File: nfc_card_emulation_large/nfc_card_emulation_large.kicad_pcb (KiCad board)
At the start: 2 copper layers, 54 x 85.7 mm, 13 parts, among them J1 Qwiic, U2 NT3H2x11

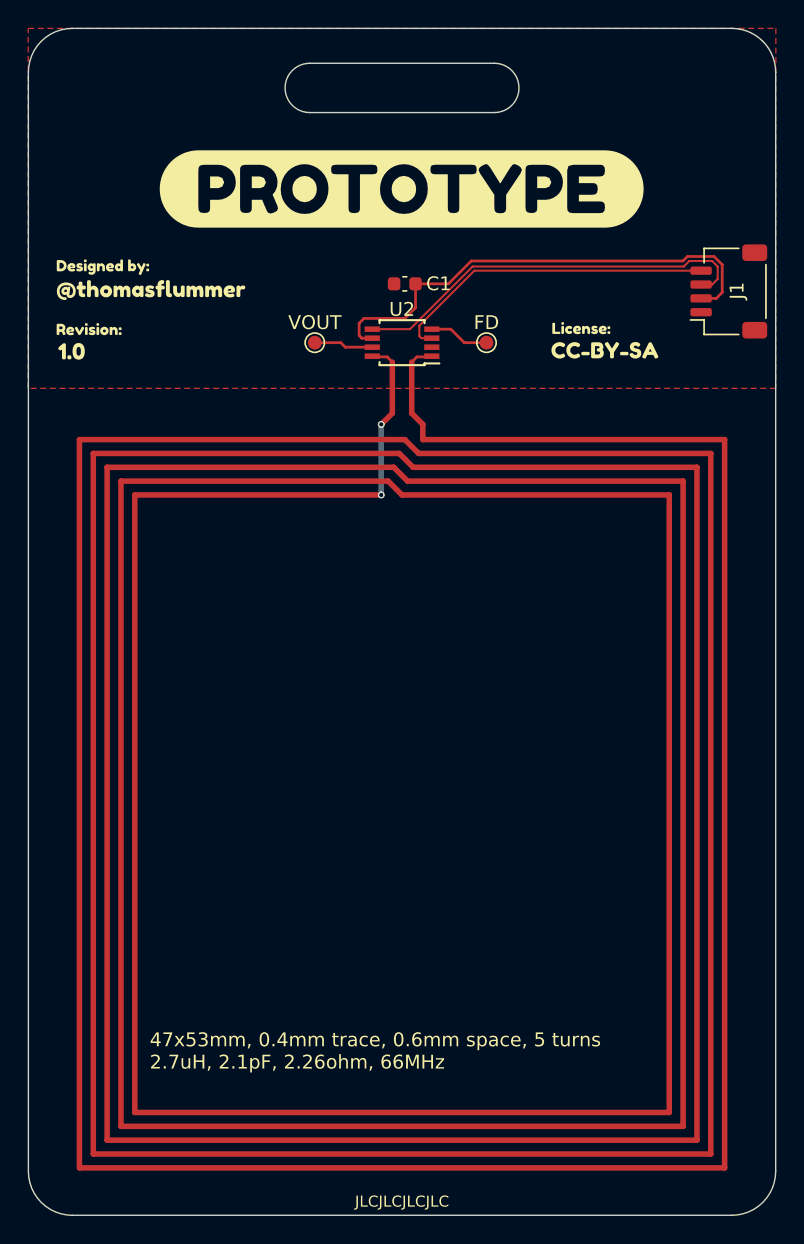
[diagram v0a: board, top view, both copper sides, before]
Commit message: Added front artwork to nfc_card_emulation_large
Also created BOM and pos files
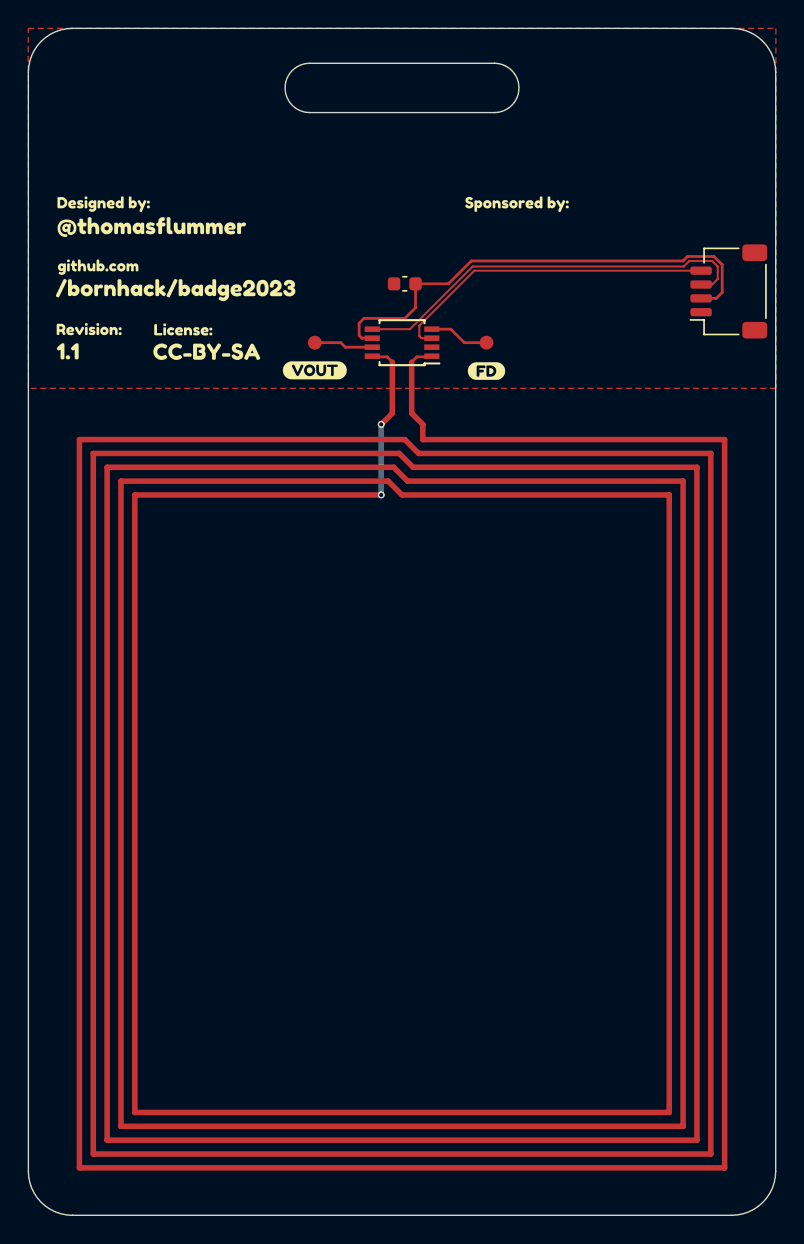
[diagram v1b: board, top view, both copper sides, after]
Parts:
- removed kibuzzard-6457B7F5: G***, kibuzzard-6457B7F5
- removed kibuzzard-645C1158: G***, kibuzzard-645C1158
- added kibuzzard-647C9608: G***, kibuzzard-647C9608, F.Cu at (58.7, 74.1)
- added kibuzzard-649468CC: G***, kibuzzard-649468CC, F.Cu at (76.6, 75.5)
- added kibuzzard-649468E2: G***, kibuzzard-649468E2, F.Cu at (89.0, 75.5)
- added kibuzzard-64946969: G***, kibuzzard-64946969, F.Cu at (60.9, 68.0)
- added kibuzzard-64946977: G***, kibuzzard-64946977, F.Cu at (66.5, 69.7)
- added kibuzzard-649469D3: G***, kibuzzard-649469D3, F.Cu at (91.2, 63.5)
- J3: renamed from J1; value Qwiic -> LCSC C145956
- U2: value NT3H2x11 -> NT3H2211
- moved kibuzzard-645C118B 28.8 mm to (67.1, 72.5)
- moved kibuzzard-645C11AA 28.8 mm to (68.8, 74.2)
- moved kibuzzard-645C104C 4.55 mm to (64.8, 65.2)
- moved kibuzzard-645C107E 4.55 mm to (61.3, 63.5)
- moved G*** 0.10 mm to (82.9, 93.6)
- renumbered C1 to C33, VOUT to TP1, FD to TP2
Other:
- board text removed: "47x53mm, 0.4mm trace, 0.6mm space, 5 turns 2.7uH, 2.1pF, 2.26ohm, 66MHz"
- board text removed: "JLCJLCJLCJLC"
